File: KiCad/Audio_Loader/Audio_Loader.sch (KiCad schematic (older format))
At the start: 22 parts, among them J1 USB_B_Micro, J2 DB9_Female_MountingHoles, J3 AudioJack2, Q1 BC547, U1 LM741, U2 LM393, U3 MAX202

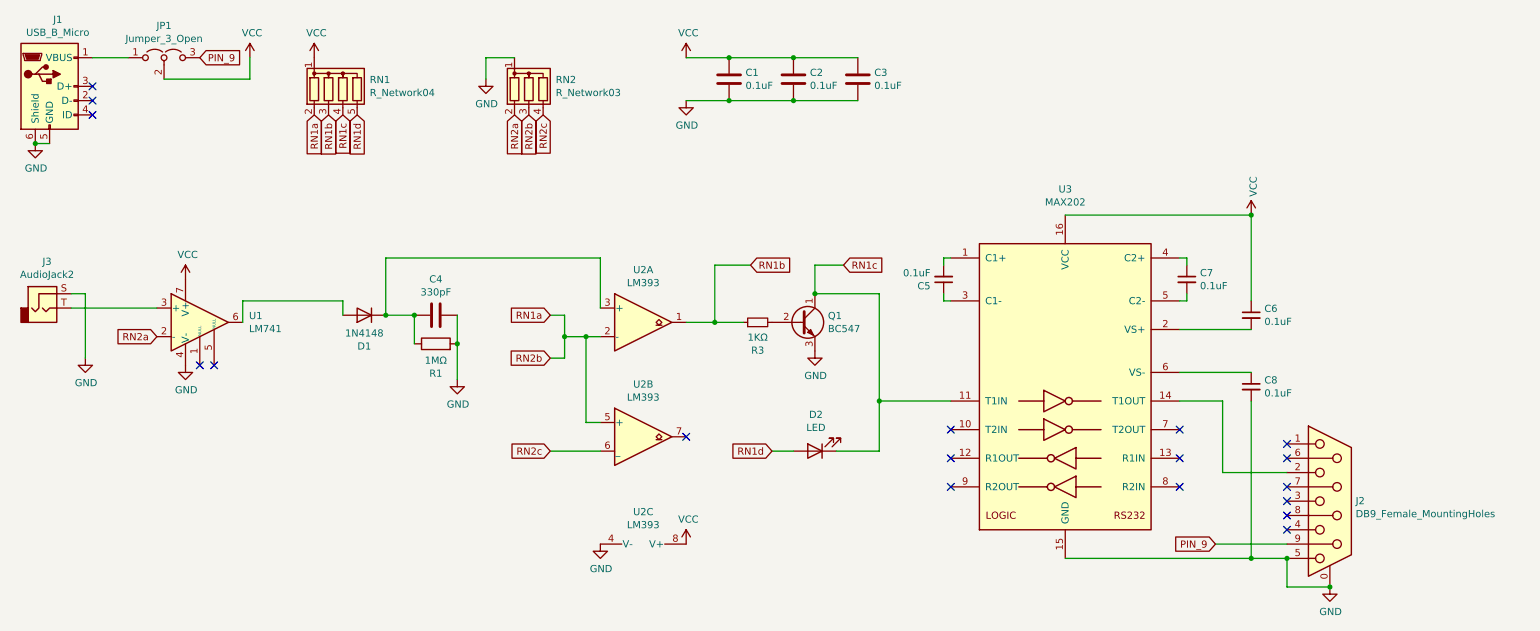
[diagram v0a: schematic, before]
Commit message: Initial commit of audio loader pcb
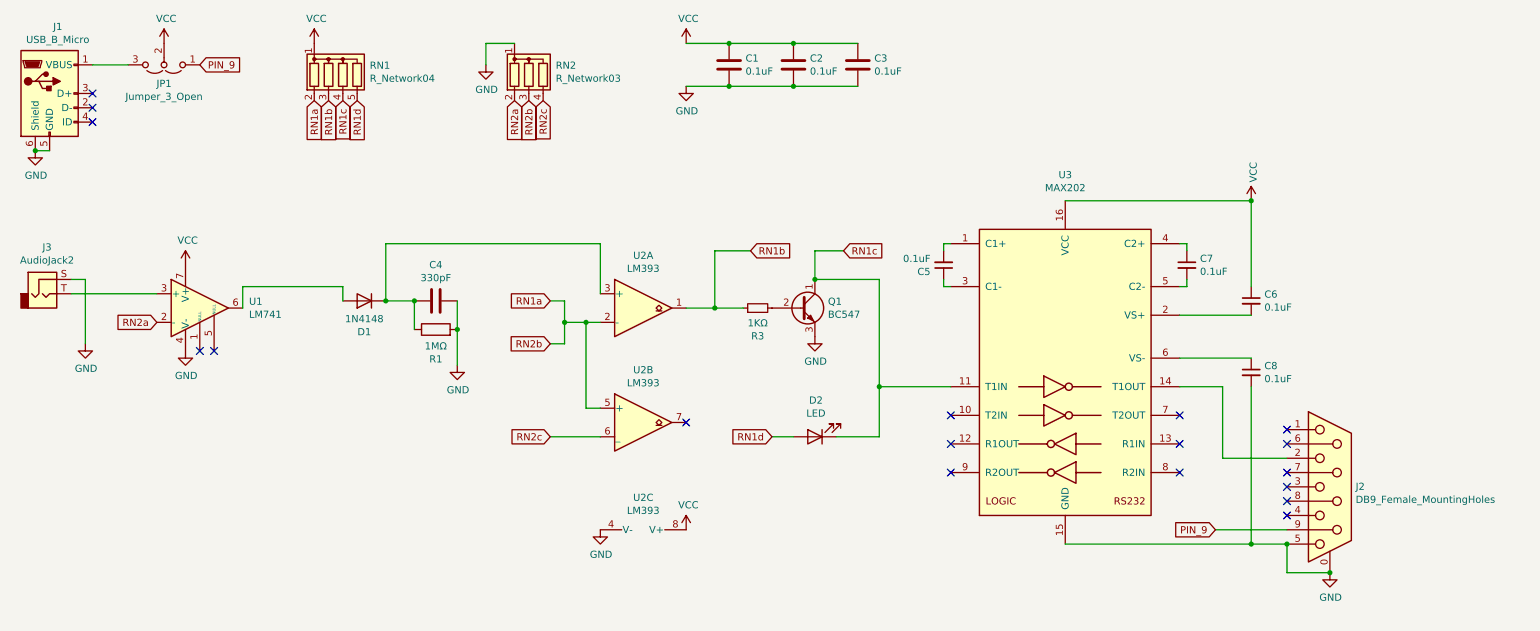
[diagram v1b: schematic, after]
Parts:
- C1, C2, C3, C4, C5, C6, C7, C8: footprint (none) -> Capacitor_THT:C_Disc_D7.5mm_W2.5mm_P5.00mm
- D2: footprint (none) -> LED_THT:LED_D5.0mm
- J1: footprint (none) -> Connector_USB:USB_Micro-AB_Molex_47590-0001
- J2: footprint (none) -> Connector_Dsub:DSUB-9_Male_Horizontal_P2.77x2.84mm_EdgePinOffset7.70mm_Housed_MountingHolesOffset9.12mm
- J3: footprint (none) -> Connector_Audio:Jack_3.5mm_CUI_SJ1-3533NG_Horizontal
- JP1: footprint (none) -> Connector_PinHeader_2.54mm:PinHeader_1x03_P2.54mm_Vertical
- R1, R3: footprint (none) -> Resistor_THT:R_Axial_DIN0207_L6.3mm_D2.5mm_P7.62mm_Horizontal
- U1, U2: footprint (none) -> Package_DIP:DIP-8_W7.62mm
- U3: footprint (none) -> Package_DIP:DIP-16_W7.62mm
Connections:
- net PIN_9: now also JP1.1 (A); no longer JP1.3 (B)
- net at J1.1 (VBUS): now also JP1.3 (B); no longer JP1.1 (A)
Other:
- moved on the sheet: C1, C2, C3, C4, C5, C6, C7, C8, D1, D2, J1, J2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

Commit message: Audio Loader PCB Rev. 0
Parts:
- J1: value USB_B_Micro -> USB PWR; footprint Connector_USB:USB_Micro-AB_Molex_47590-0001 -> Connector_USB:USB_Micro-B_Amphenol_10118194_Horizontal
- J2: value DB9_Female_MountingHoles -> DE-9 Female; footprint Connector_Dsub:DSUB-9_Male_Horizontal_P2.77x2.84mm_EdgePinOffset7.70mm_Housed_MountingHolesOffset9.12mm -> Connector_Dsub:DSUB-9_Female_Horizontal_P2.77x2.84mm_EdgePinOffset4.94mm_Housed_MountingHolesOffset7.48mm
- J3: value AudioJack2 -> TS Jack
- Q1: footprint Package_TO_SOT_THT:TO-92_Inline -> Package_TO_SOT_THT:TO-92_Inline_Wide
- RN1: value R_Network04 -> 1KΩ
- RN2: value R_Network03 -> 1KΩ
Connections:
- net RN1a: now also RN1.5 (R4); no longer RN1.2 (R1)
- net RN1b: now also RN1.4 (R3); no longer RN1.3 (R2)
- net RN1c: now also RN1.2 (R1); no longer RN1.4 (R3)
- net RN1d: now also RN1.3 (R2); no longer RN1.5 (R4)
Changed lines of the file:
@@
-$EndComp
-$Comp
-L Transistor_BJT:BC547 Q1
-U 1 1 6193E030
-P 6200 2950
-F 0 "Q1" H 6391 2996 50  0000 L CNN
-F 1 "BC547" H 6391 2905 50  0000 L CNN
-F 2 "Package_TO_SOT_THT:TO-92_Inline" H 6400 2875 50  0001 L CIN
-F 3 "https://www.onsemi.com/pub/Collateral/BC550-D.pdf" H 6200 2950 50  0001 L CNN
-	1    6200 2950
-	1    0    0    -1
 $EndComp
 $Comp
@@
 P 950 1450
 F 0 "J1" H 1007 1917 50  0000 C CNN
-F 1 "USB_B_Micro" H 1007 1826 50  0000 C CNN
-F 2 "Connector_USB:USB_Micro-AB_Molex_47590-0001" H 1100 1400 50  0001 C CNN
+F 1 "USB PWR" H 1007 1826 50  0000 C CNN
+F 2 "Connector_USB:USB_Micro-B_Amphenol_10118194_Horizontal" H 1100 1400 50  0001 C CNN
 F 3 "~" H 1100 1400 50  0001 C CNN
 	1    950  1450
@@
 Wire Wire Line
 	6300 2550 6300 2750
-Connection ~ 6300 2750
 Text GLabel 6000 3850 0    50   Input ~ 0
 RN1d
@@
 Wire Wire Line
 	5400 1400 5700 1400
+Text GLabel 2900 1500 3    50   Input ~ 0
+RN1d
+Text GLabel 2800 1500 3    50   Input ~ 0
+RN1c
+Text GLabel 3000 1500 3    50   Input ~ 0
+RN1b
 Text GLabel 3100 1500 3    50   Input ~ 0
-RN1d
-Text GLabel 3000 1500 3    50   Input ~ 0
-RN1c
-Text GLabel 2900 1500 3    50   Input ~ 0
-RN1b
-Text GLabel 2800 1500 3    50   Input ~ 0
 RN1a
 $Comp
@@
 P 3000 1300
 F 0 "RN1" H 3188 1346 50  0000 L CNN
-F 1 "R_Network04" H 3188 1255 50  0000 L CNN
+F 1 "1KΩ" H 3188 1255 50  0000 L CNN
 F 2 "Resistor_THT:R_Array_SIP5" V 3275 1300 50  0001 C CNN
 F 3 "http://www.vishay.com/docs/31509/csc.pdf" H 3000 1300 50  0001 C CNN
@@
 P 9900 4200
 F 0 "J2" H 10080 4202 50  0000 L CNN
-F 1 "DB9_Female_MountingHoles" H 10080 4111 50  0000 L CNN
-F 2 "Connector_Dsub:DSUB-9_Male_Horizontal_P2.77x2.84mm_EdgePinOffset7.70mm_Housed_MountingHolesOffset9.12mm" H 9900 4200 50  0001 C CNN
+F 1 "DE-9 Female" H 10080 4111 50  0000 L CNN
+F 2 "Connector_Dsub:DSUB-9_Female_Horizontal_P2.77x2.84mm_EdgePinOffset4.94mm_Housed_MountingHolesOffset7.48mm" H 9900 4200 50  0001 C CNN
 F 3 " ~" H 9900 4200 50  0001 C CNN
 	1    9900 4200
@@
 P 900 2850
 F 0 "J3" H 932 3175 50  0000 C CNN
-F 1 "AudioJack2" H 932 3084 50  0000 C CNN
+F 1 "TS Jack" H 932 3084 50  0000 C CNN
 F 2 "Connector_Audio:Jack_3.5mm_CUI_SJ1-3533NG_Horizontal" H 900 2850 50  0001 C CNN
 F 3 "~" H 900 2850 50  0001 C CNN
@@
 P 4300 1300
 F 0 "RN2" H 4488 1346 50  0000 L CNN
-F 1 "R_Network03" H 4488 1255 50  0000 L CNN
+F 1 "1KΩ" H 4488 1255 50  0000 L CNN
 F 2 "Resistor_THT:R_Array_SIP4" V 4575 1300 50  0001 C CNN
 F 3 "http://www.vishay.com/docs/31509/csc.pdf" H 4300 1300 50  0001 C CNN
@@
 	1    0    0    -1
 $EndComp
+Connection ~ 6300 2750
+$Comp
+L Transistor_BJT:BC547 Q1
+U 1 1 6193E030
+P 6200 2950
+F 0 "Q1" H 6391 2996 50  0000 L CNN
+F 1 "BC547" H 6391 2905 50  0000 L CNN
+F 2 "Package_TO_SOT_THT:TO-92_Inline_Wide" H 6400 2875 50  0001 L CIN
+F 3 "https://www.onsemi.com/pub/Collateral/BC550-D.pdf" H 6200 2950 50  0001 L CNN
+	1    6200 2950
+	1    0    0    -1
+$EndComp
